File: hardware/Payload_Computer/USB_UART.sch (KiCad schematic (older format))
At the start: 1 part

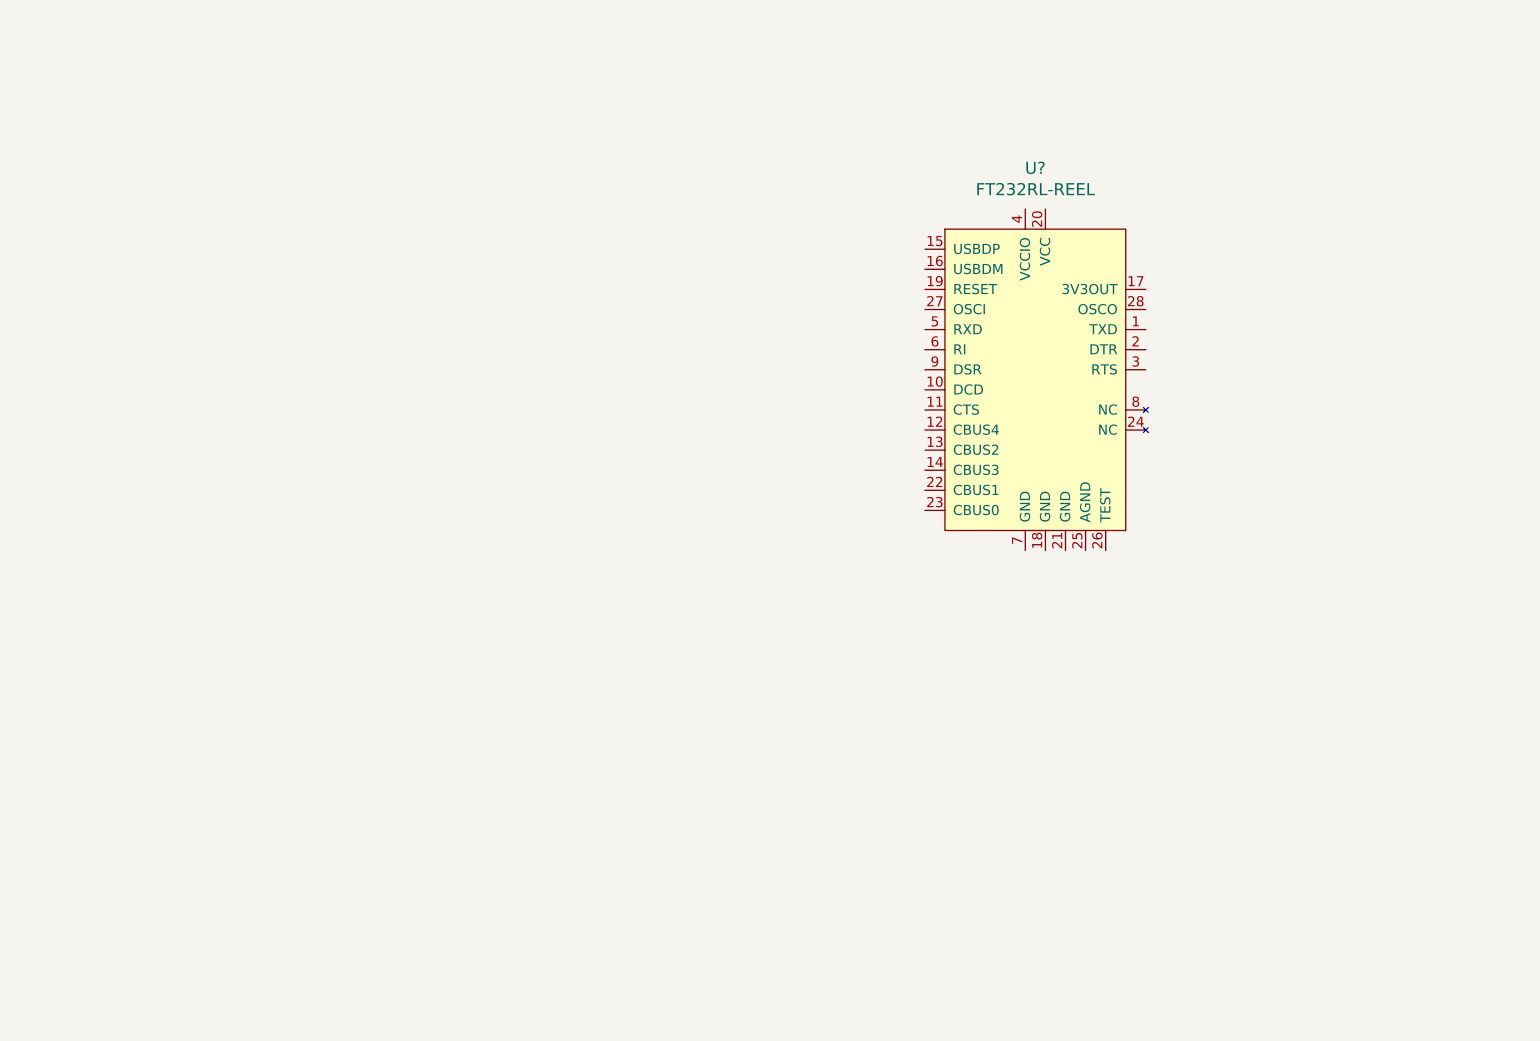
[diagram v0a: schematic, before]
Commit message: Added FTDI
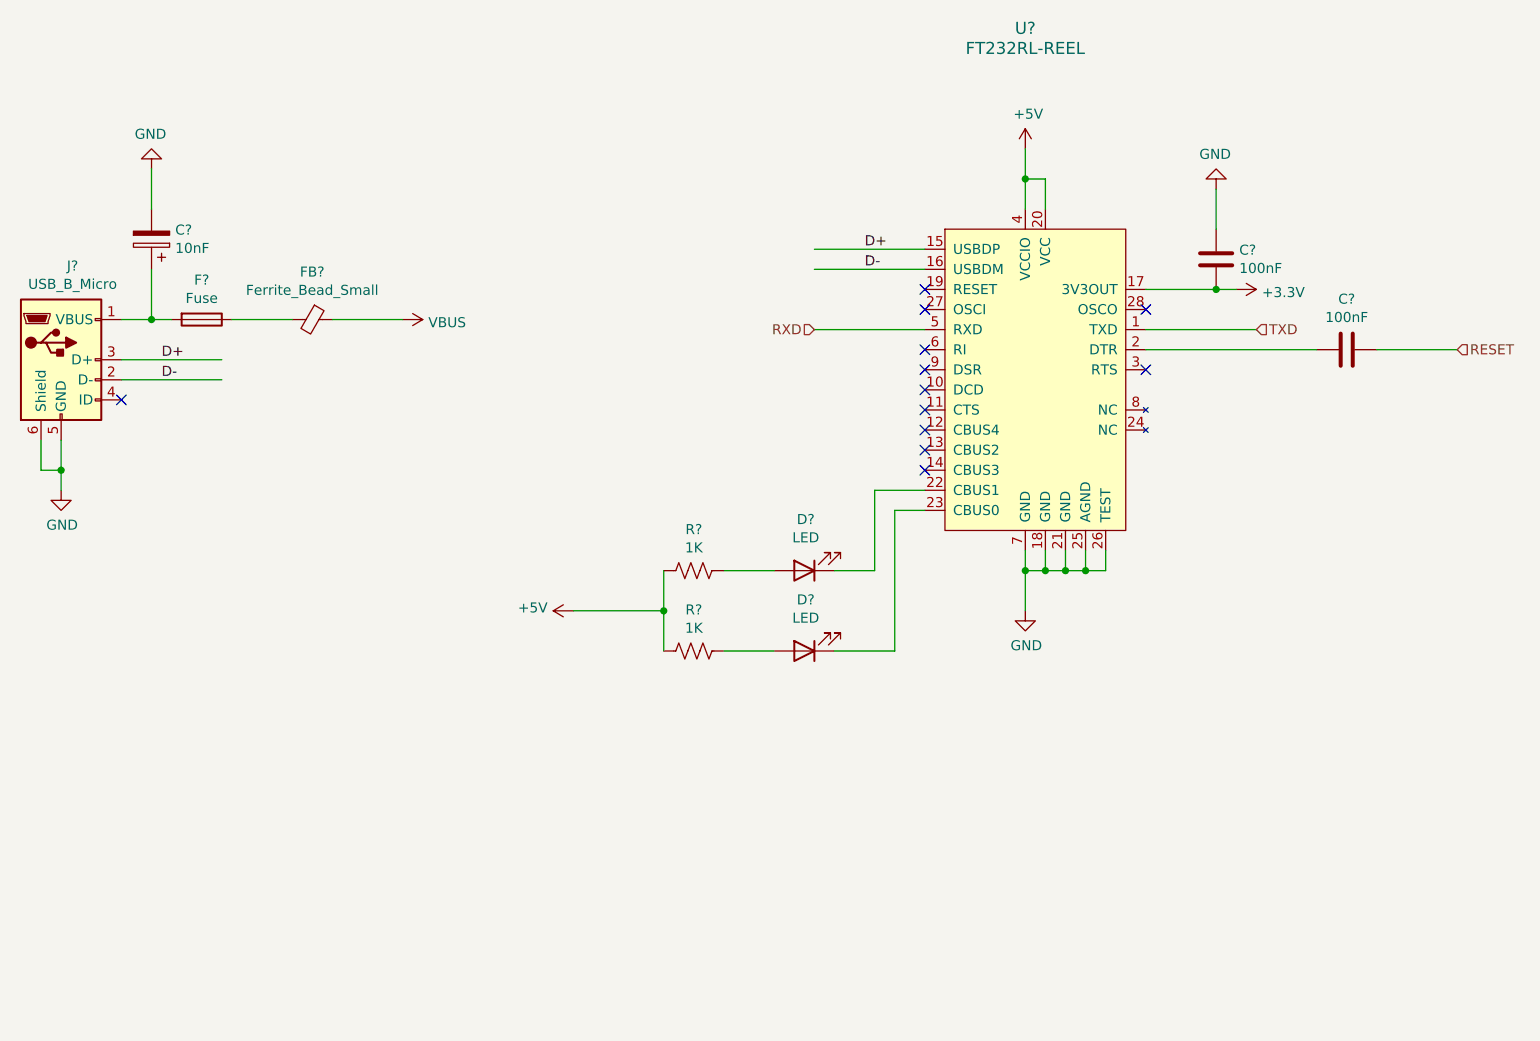
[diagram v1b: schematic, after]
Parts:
- added C?: 10nF, symbol Device:CP
- added C? (x2): 100nF, symbol Device:C
- added D? (x2): LED, symbol Device:LED
- added F?: Fuse, symbol Device:Fuse
- added FB?: Ferrite_Bead_Small, symbol Device:Ferrite_Bead_Small
- added J?: USB_B_Micro, symbol Connector:USB_B_Micro
- added R? (x2): 1K, symbol Device:R_US
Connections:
- net labels added: +3.3V, +5V, D+, D-, GND, RESET, RXD, TXD, VBUS
- wire segments 0 -> 46
- no-connect marks 0 -> 12

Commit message: Added reset circuits
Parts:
- added R? (x2): 1K, symbol Device:R_US
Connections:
- wire segments 46 -> 50
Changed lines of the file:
@@
 $Descr A4 11693 8268
 encoding utf-8
-Sheet 6 7
+Sheet 6 9
 Title ""
 Date ""
@@
 Text Label 6050 2800 0    50   ~ 0
 D-
-Text HLabel 5800 3100 0    50   Input ~ 0
+Text HLabel 5250 3100 0    50   Input ~ 0
 RXD
-Text HLabel 8000 3100 2    50   Input ~ 0
+Text HLabel 9000 2750 2    50   Input ~ 0
 TXD
-Wire Wire Line
-	7450 3100 8000 3100
 Wire Wire Line
 	6350 3100 5800 3100
@@
 NoConn ~ 6350 3700
 NoConn ~ 6350 3800
+$Comp
+L Device:R_US R?
+U 1 1 5F8E2EB9
+P 5650 3100
+F 0 "R?" V 5445 3100 50  0000 C CNN
+F 1 "1K" V 5536 3100 50  0000 C CNN
+F 2 "" V 5690 3090 50  0001 C CNN
+F 3 "~" H 5650 3100 50  0001 C CNN
+	1    5650 3100
+	0    1    1    0
+$EndComp
+Wire Wire Line
+	5500 3100 5250 3100
+Wire Wire Line
+	8300 3100 8300 2750
+Wire Wire Line
+	8300 2750 8450 2750
+Wire Wire Line
+	7450 3100 8300 3100
+$Comp
+L Device:R_US R?
+U 1 1 5F8E4F1C
+P 8600 2750
+F 0 "R?" V 8395 2750 50  0000 C CNN
+F 1 "1K" V 8486 2750 50  0000 C CNN
+F 2 "" V 8640 2740 50  0001 C CNN
+F 3 "~" H 8600 2750 50  0001 C CNN
+	1    8600 2750
+	0    1    1    0
+$EndComp
+Wire Wire Line
+	8750 2750 9000 2750
 $EndSCHEMATC

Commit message: Finished ICSP. Added a few leds and filtering caps
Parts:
- added C?: 100 nF, symbol Device:C
- added C?: 4.7 uF, symbol Device:CP
- FB?: value Ferrite_Bead_Small -> 600 OHM
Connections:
- wire segments 50 -> 58
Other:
- note added: "PLACE NEAR FTDI POWER INPUT\n"
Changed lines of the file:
@@
 $Descr A4 11693 8268
 encoding utf-8
-Sheet 6 11
+Sheet 6 13
 Title ""
 Date ""
@@
 	2500 3050 2600 3050
 $Comp
-L power:GND #PWR?
+L power:GND #PWR0109
 U 1 1 5F858C58
 P 2500 2300
-F 0 "#PWR?" H 2500 2050 50  0001 C CNN
+F 0 "#PWR0109" H 2500 2050 50  0001 C CNN
 F 1 "GND" H 2505 2127 50  0000 C CNN
 F 2 "" H 2500 2300 50  0001 C CNN
@@
 P 3300 3050
 F 0 "FB?" V 3063 3050 50  0000 C CNN
-F 1 "Ferrite_Bead_Small" V 3154 3050 50  0000 C CNN
+F 1 "600 OHM" V 3154 3050 50  0000 C CNN
 F 2 "" V 3230 3050 50  0001 C CNN
 F 3 "~" H 3300 3050 50  0001 C CNN
@@
 	2900 3050 3200 3050
 $Comp
-L power:VBUS #PWR?
+L power:VBUS #PWR0110
 U 1 1 5F859D37
 P 3750 3050
-F 0 "#PWR?" H 3750 2900 50  0001 C CNN
+F 0 "#PWR0110" H 3750 2900 50  0001 C CNN
 F 1 "VBUS" V 3765 3178 50  0000 L CNN
 F 2 "" H 3750 3050 50  0001 C CNN
@@
 	3400 3050 3750 3050
 $Comp
-L power:GND #PWR?
+L power:GND #PWR0111
 U 1 1 5F85A3C3
 P 2050 3900
-F 0 "#PWR?" H 2050 3650 50  0001 C CNN
+F 0 "#PWR0111" H 2050 3650 50  0001 C CNN
 F 1 "GND" H 2055 3727 50  0000 C CNN
 F 2 "" H 2050 3900 50  0001 C CNN
@@
 NoConn ~ 2350 3450
 $Comp
-L power:+5V #PWR?
+L power:+5V #PWR0112
 U 1 1 5F85B744
 P 6850 2200
-F 0 "#PWR?" H 6850 2050 50  0001 C CNN
+F 0 "#PWR0112" H 6850 2050 50  0001 C CNN
 F 1 "+5V" H 6865 2373 50  0000 C CNN
 F 2 "" H 6850 2200 50  0001 C CNN
@@
 	6850 2350 6850 2200
 $Comp
-L power:GND #PWR?
+L power:GND #PWR0113
 U 1 1 5F85C222
 P 6850 4500
-F 0 "#PWR?" H 6850 4250 50  0001 C CNN
+F 0 "#PWR0113" H 6850 4250 50  0001 C CNN
 F 1 "GND" H 6855 4327 50  0000 C CNN
 F 2 "" H 6850 4500 50  0001 C CNN
@@
 	7450 2900 7800 2900
 $Comp
-L power:+3.3V #PWR?
+L power:+3.3V #PWR0114
 U 1 1 5F863614
 P 7900 2900
-F 0 "#PWR?" H 7900 2750 50  0001 C CNN
+F 0 "#PWR0114" H 7900 2750 50  0001 C CNN
 F 1 "+3.3V" V 7915 3028 50  0000 L CNN
 F 2 "" H 7900 2900 50  0001 C CNN
@@
 Connection ~ 7800 2900
 $Comp
-L power:GND #PWR?
+L power:GND #PWR0115
 U 1 1 5F8647C2
 P 7800 2400
-F 0 "#PWR?" H 7800 2150 50  0001 C CNN
+F 0 "#PWR0115" H 7800 2150 50  0001 C CNN
 F 1 "GND" H 7805 2227 50  0000 C CNN
 F 2 "" H 7800 2400 50  0001 C CNN
@@
 	5600 4700 5350 4700
 $Comp
-L power:+5V #PWR?
+L power:+5V #PWR0116
 U 1 1 5F869AE2
 P 4600 4500
-F 0 "#PWR?" H 4600 4350 50  0001 C CNN
+F 0 "#PWR0116" H 4600 4350 50  0001 C CNN
 F 1 "+5V" V 4615 4628 50  0000 L CNN
 F 2 "" H 4600 4500 50  0001 C CNN
@@
 Wire Wire Line
 	8750 2750 9000 2750
+$Comp
+L Device:C C?
+U 1 1 5F992766
+P 3050 5800
+F 0 "C?" H 3165 5846 50  0000 L CNN
+F 1 "100 nF" H 3165 5755 50  0000 L CNN
+F 2 "" H 3088 5650 50  0001 C CNN
+F 3 "~" H 3050 5800 50  0001 C CNN
+	1    3050 5800
+	1    0    0    -1
+$EndComp
+$Comp
+L Device:CP C?
+U 1 1 5F99276C
+P 2600 5800
+F 0 "C?" H 2718 5846 50  0000 L CNN
+F 1 "4.7 uF" H 2718 5755 50  0000 L CNN
+F 2 "" H 2638 5650 50  0001 C CNN
+F 3 "~" H 2600 5800 50  0001 C CNN
+	1    2600 5800
+	1    0    0    -1
+$EndComp
+$Comp
+L power:+5V #PWR?
+U 1 1 5F992772
+P 2800 5250
+F 0 "#PWR?" H 2800 5100 50  0001 C CNN
+F 1 "+5V" H 2815 5423 50  0000 C CNN
+F 2 "" H 2800 5250 50  0001 C CNN
+F 3 "" H 2800 5250 50  0001 C CNN
+	1    2800 5250
+	1    0    0    -1
+$EndComp
+Wire Wire Line
+	2600 5650 2600 5250
+Wire Wire Line
+	2600 5250 2800 5250
+Wire Wire Line
+	3050 5650 3050 5250
+Wire Wire Line
+	3050 5250 2800 5250
+Connection ~ 2800 5250
+$Comp
+L power:GND #PWR?
+U 1 1 5F99277D
+P 2800 6150
+F 0 "#PWR?" H 2800 5900 50  0001 C CNN
+F 1 "GND" H 2805 5977 50  0000 C CNN
+F 2 "" H 2800 6150 50  0001 C CNN
+F 3 "" H 2800 6150 50  0001 C CNN
+	1    2800 6150
+	1    0    0    -1
+$EndComp
+Wire Wire Line
+	2600 5950 2600 6150
+Wire Wire Line
+	2600 6150 2800 6150
+Wire Wire Line
+	3050 5950 3050 6150
+Wire Wire Line
+	3050 6150 2800 6150
+Connection ~ 2800 6150
+Text Notes 2250 6550 0    50   ~ 0
+PLACE NEAR FTDI POWER INPUT\n
 $EndSCHEMATC
